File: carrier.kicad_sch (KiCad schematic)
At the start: 41 parts, among them J1 Conn_02x06_Odd_Even, J10 Conn_01x02, J2 Conn_01x26, J3 Conn_01x26, J4 TYPE-C-31-M-12, J5 Conn_01x02, J6 Conn_01x02, J7 Conn_01x02, J8 Conn_01x02, J9 Conn_01x02, U1 CARAVEL, U2 W25Q128JVS, U3 LP5907MFX-3.3, U4 LP5907MFX-1.8, U5 LP5907MFX-1.8, U6 LP5907MFX-3.3, U7 TPD2E001DRSR, X1 SG-5032CAN

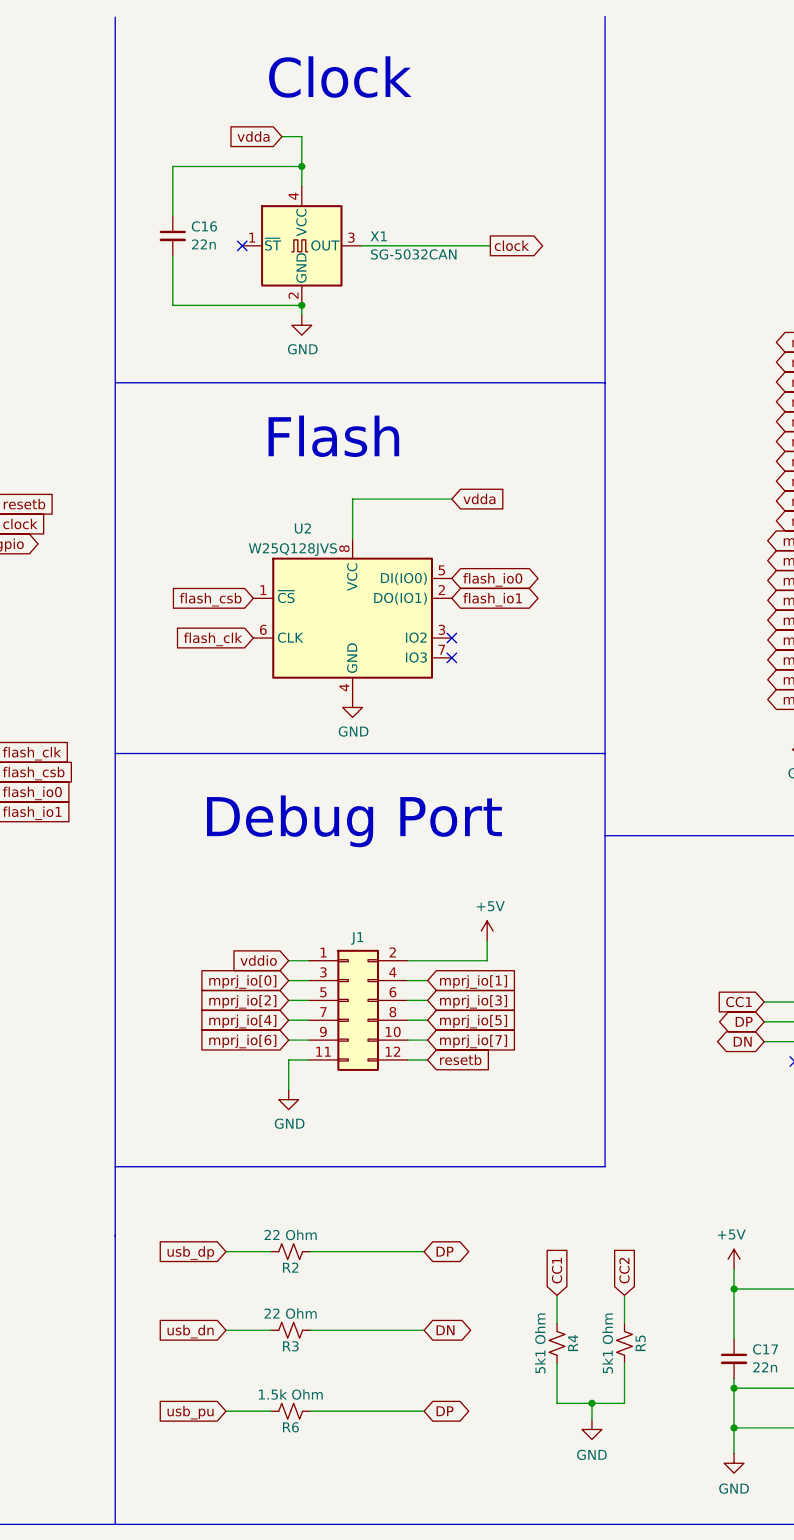
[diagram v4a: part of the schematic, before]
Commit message: Add provision for external clk on  pin header
Uses a solder jumper to select oscillator by default.
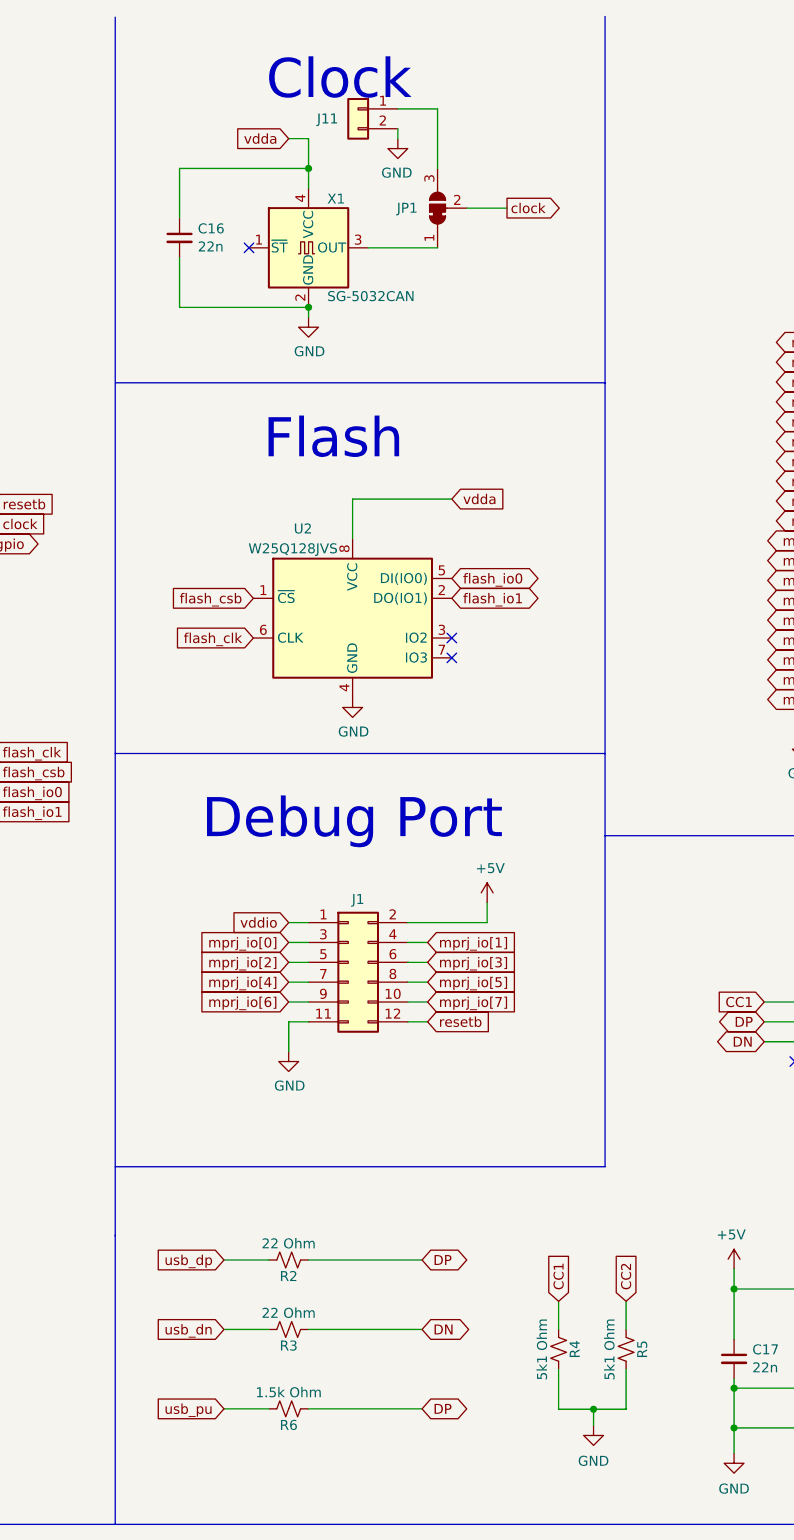
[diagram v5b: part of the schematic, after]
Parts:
- added J11: Conn_01x02, Connector_PinHeader_2.54mm:PinHeader_1x02_P2.54mm_Vertical, symbol Connector_Generic:Conn_01x02
- added JP1: SolderJumper_3_Bridged12, Jumper:SolderJumper-3_P1.3mm_Bridged12_Pad1.0x1.5mm, symbol Jumper:SolderJumper_3_Bridged12
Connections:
- net GND: now also J11.2 (Pin_2)
- net clock: now also JP1.2 (C); no longer X1.3 (OUT)
- new net: JP1.1 (A), X1.3 (OUT)
- new net: J11.1 (Pin_1), JP1.3 (B)
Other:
- moved on the sheet: C16, J1, R2, R4, R5, X1

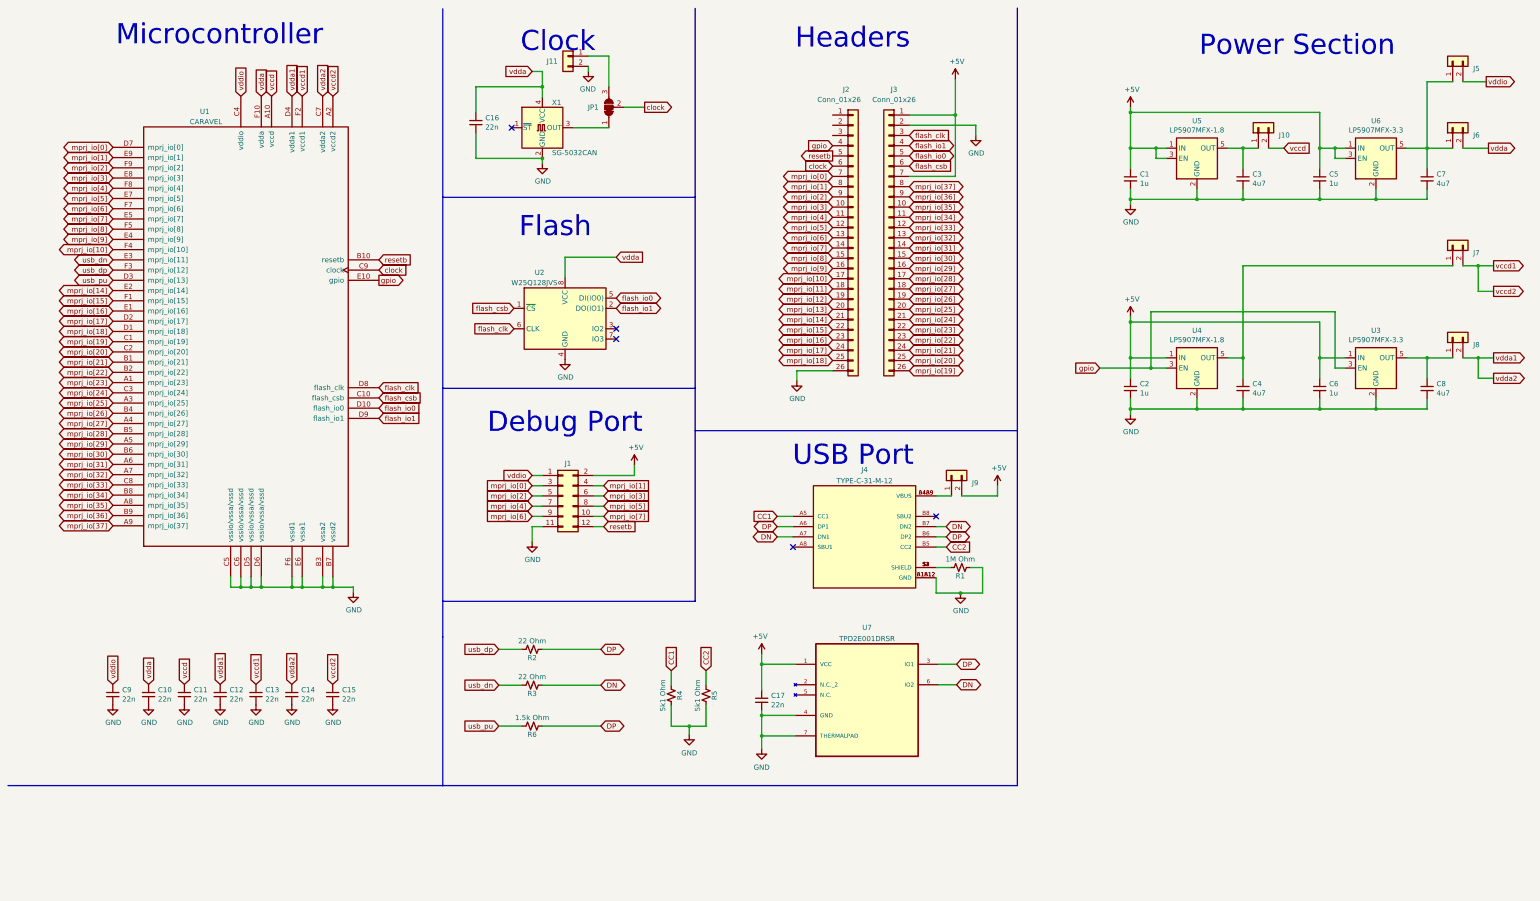
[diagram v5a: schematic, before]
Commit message: Add audio circuitry
Adds headphone output for the PCM audio output
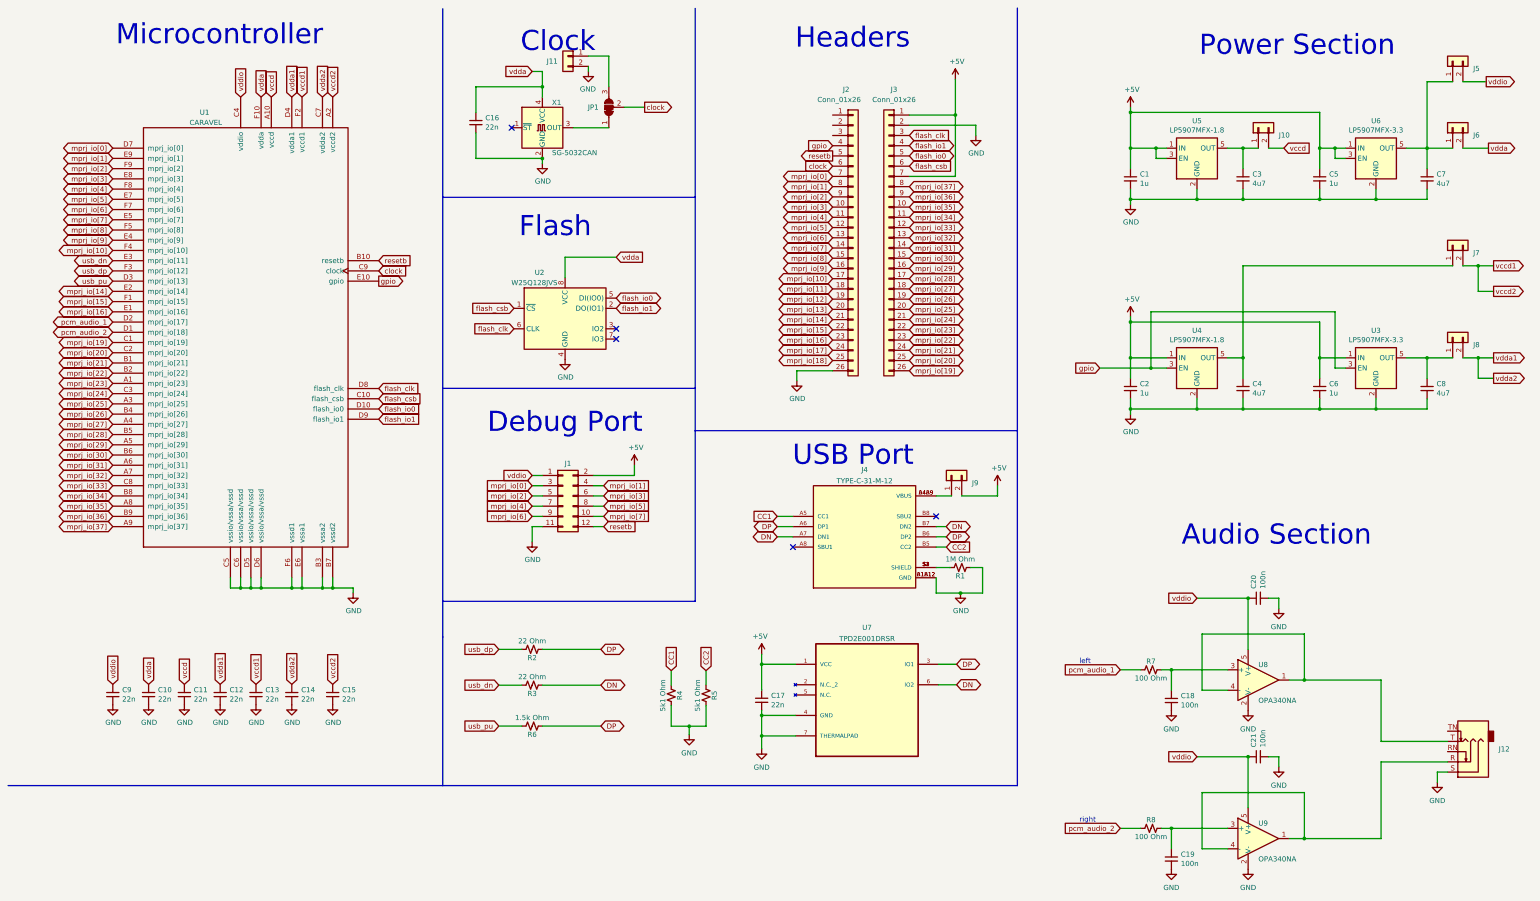
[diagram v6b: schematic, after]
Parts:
- added C18, C19, C20, C21: 100n, Capacitor_SMD:C_0402_1005Metric, symbol Device:C_Small
- added J12: AudioJack3_SwitchTR, Connector_Audio:Jack_3.5mm_CUI_SJ1-3535NG_Horizontal_CircularHoles, symbol Connector:AudioJack3_SwitchTR
- added R7, R8: 100 Ohm, Resistor_SMD:R_0402_1005Metric, symbol Device:R_Small_US
- added U8, U9: OPA340NA, Package_TO_SOT_SMD:SOT-23-5, symbol Amplifier_Operational:OPA340NA
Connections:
- net GND: now also C18.2, C19.2, C20.2, C21.2, J12.S, U8.2 (V-), U9.2 (V-)
- net mprj_io[17]: no longer U1.D2 (mprj_io[17])
- net mprj_io[18]: no longer U1.D1 (mprj_io[18])
- net vddio: now also C20.1, C21.1, U8.5 (V+), U9.5 (V+)
- new net: J12.R, U9.1, U9.4 (-)
- new net: C19.1, R8.1, U9.3 (+)
- new net: C18.1, R7.1, U8.3 (+)
- new net: J12.T, U8.1, U8.4 (-)
- new net pcm_audio_1: R7.2, U1.D2 (mprj_io[17])
- new net pcm_audio_2: R8.2, U1.D1 (mprj_io[18])
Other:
- note added: "Audio Section"
- note added: "left"
- note added: "right"

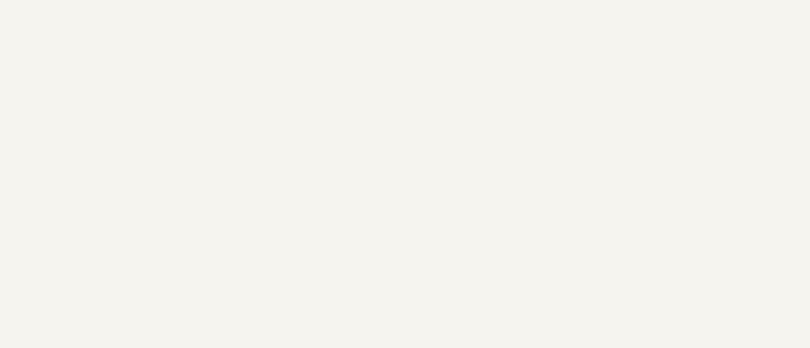
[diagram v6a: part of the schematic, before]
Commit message: Add GND hook test point
Might want to add more test points for various things.
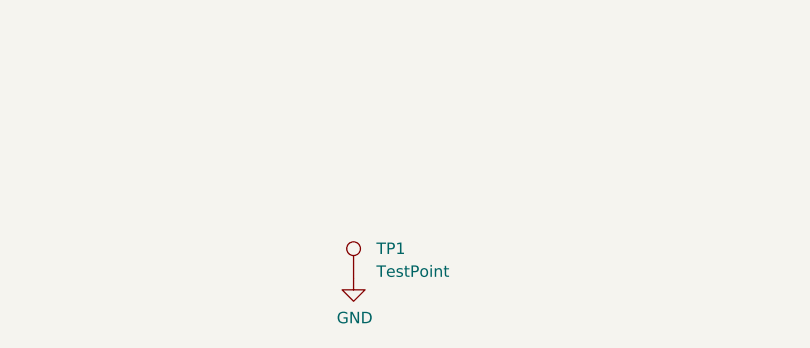
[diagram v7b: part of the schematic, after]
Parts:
- added TP1: TestPoint, TestPoint:TestPoint_Keystone_5000-5004_Miniature, symbol Connector:TestPoint
- U7: footprint SON95P315X315X80-7N -> TPD2E001DRSR:SON95P315X315X80-7N
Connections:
- net GND: now also TP1.1
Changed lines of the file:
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@@
+    (pin "1")
+  )
+  (symbol (lib_id "Connector:TestPoint") (at 63.5 243.84 0) (unit 1)
+    (in_bom yes) (on_board yes) (fields_autoplaced)
+    (property "Reference" "TP1" (id 0) (at 66.04 240.5379 0)
+      (effects (font (size 1.27 1.27)) (justify left))
+    )
+    (property "Value" "TestPoint" (id 1) (at 66.04 243.0779 0)
+      (effects (font (size 1.27 1.27)) (justify left))
+    )
+    (property "Footprint" "TestPoint:TestPoint_Keystone_5000-5004_Miniature" (id 2) (at 68.58 243.84 0)
+      (effects (font (size 1.27 1.27)) hide)
+    )
+    (property "Datasheet" "~" (id 3) (at 68.58 243.84 0)
+      (effects (font (size 1.27 1.27)) hide)
+    )
     (pin "1")
   )
@@
     )
     (property "Datasheet" "" (id 3) (at 55.88 185.2168 0)
+      (effects (font (size 1.27 1.27)) hide)
+    )
+    (pin "1")
+  )
+  (symbol (lib_id "power:GND") (at 63.5 243.84 0) (unit 1)
+    (in_bom yes) (on_board yes)
+    (property "Reference" "#PWR0113" (id 0) (at 63.5 250.19 0)
+      (effects (font (size 1.27 1.27)) hide)
+    )
+    (property "Value" "GND" (id 1) (at 63.627 248.2342 0))
+    (property "Footprint" "" (id 2) (at 63.5 243.84 0)
+      (effects (font (size 1.27 1.27)) hide)
+    )
+    (property "Datasheet" "" (id 3) (at 63.5 243.84 0)
       (effects (font (size 1.27 1.27)) hide)
     )
@@
     (property "Reference" "U7" (id 0) (at 225.3996 166.0356 0))
     (property "Value" "TPD2E001DRSR" (id 1) (at 225.3996 168.8107 0))
-    (property "Footprint" "SON95P315X315X80-7N" (id 2) (at 225.3996 180.2384 0)
+    (property "Footprint" "TPD2E001DRSR:SON95P315X315X80-7N" (id 2) (at 225.3996 180.2384 0)
       (effects (font (size 1.27 1.27)) (justify left bottom) hide)
     )
@@
       (reference "#PWR0112") (unit 1) (value "+5V") (footprint "")
     )
+    (path "/39c779ab-5994-483e-bbf8-ea53ed5d1221"
+      (reference "#PWR0113") (unit 1) (value "GND") (footprint "")
+    )
     (path "/00000000-0000-0000-0000-00005fbcd24e"
       (reference "C1") (unit 1) (value "1u") (footprint "Capacitor_SMD:C_0603_1608Metric")
@@
       (reference "R8") (unit 1) (value "100 Ohm") (footprint "Resistor_SMD:R_0402_1005Metric")
     )
+    (path "/15d7dfee-2a57-46bf-9451-855be6f04a7a"
+      (reference "TP1") (unit 1) (value "TestPoint") (footprint "TestPoint:TestPoint_Keystone_5000-5004_Miniature")
+    )
     (path "/00000000-0000-0000-0000-00005fb81f59"
       (reference "U1") (unit 1) (value "CARAVEL") (footprint "carrier:WLCSP-60_P0.5mm")
@@
     )
     (path "/e7a6a157-7dfa-42f3-a79b-bc46506af3bf"
-      (reference "U7") (unit 1) (value "TPD2E001DRSR") (footprint "SON95P315X315X80-7N")
+      (reference "U7") (unit 1) (value "TPD2E001DRSR") (footprint "TPD2E001DRSR:SON95P315X315X80-7N")
     )
     (path "/9995eaa8-0f1b-4ed0-8995-c367b668896d"
